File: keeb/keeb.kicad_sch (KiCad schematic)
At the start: 161 parts, among them J101 AVR-ISP-6, J102 USB_C_Receptacle_USB2.0, SW101 SW_Push, SW102 SW_Push, SW103 SW_Push, SW104 SW_Push, SW105 SW_Push, SW106 SW_Push, SW107 SW_Push, SW108 SW_Push, SW109 SW_Push, SW110 SW_Push, SW111 SW_Push, SW112 SW_Push, SW113 SW_Push, SW114 SW_Push, SW115 SW_Push, SW116 SW_Push, SW117 SW_Push, SW118 SW_Push, SW119 SW_Push, SW120 SW_Push, SW121 SW_Push, SW122 SW_Push, SW123 SW_Push, SW124 SW_Push, SW125 SW_Push, SW126 SW_Push, SW127 SW_Push, SW128 SW_Push, SW129 SW_Push, SW130 SW_Push, SW131 SW_Push, SW132 SW_Push, SW133 SW_Push, SW134 SW_Push, SW135 SW_Push, SW136 SW_Push, SW137 SW_Push, SW138 SW_Push, SW139 SW_Push, SW140 SW_Push, SW141 SW_Push, SW142 SW_Push, SW143 SW_Push, SW144 SW_Push, SW145 SW_Push, SW146 SW_Push, SW147 SW_Push, SW148 SW_Push, SW149 SW_Push, SW150 SW_Push, SW151 SW_Push, SW152 SW_Push, SW153 SW_Push, SW154 SW_Push, SW155 SW_Push, SW156 SW_Push, SW157 SW_Push, SW158 SW_Push, SW159 SW_Push, SW160 SW_Push, SW161 SW_Push, SW162 SW_Push, SW163 SW_Push, SW164 SW_Push, SW165 SW_Push, SW166 SW_Push, SW167 SW_Push, U101 ATmega32U4-AU, Y101 16Mhz

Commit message: clean trace
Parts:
- I2C_101, I2C_102: Supplier # (none) -> digi: 839-54-00177CT-ND
- J101: man# digi:839-54-00177CT-ND -> (none)
- J102: Supplier # (none) -> LCSC: C165948; man# LCSC: C165948 -> (none)
- SW101: Supplier # (none) -> LCSC: C231329
- U101: symbol keeb-rescue:ATmega32U4-AU-MCU_Microchip_ATmega -> MCU_Microchip_ATmega:ATmega32U4RC-A; Supplier # (none) -> digi: ATMEGA32U4RC-AU-ND
- Y101: Supplier # (none) -> LCSC: C431146
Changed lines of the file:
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@@
     (pin "2")
   )
-  (symbol (lib_id "keeb-rescue:ATmega32U4-AU-MCU_Microchip_ATmega") (at 228.6 104.775 0) (unit 1)
+  (symbol (lib_id "MCU_Microchip_ATmega:ATmega32U4RC-A") (at 228.6 104.775 0) (unit 1)
     (in_bom yes) (on_board yes)
     (property "Reference" "U101" (id 0) (at 232.41 149.86 0))
@@
     )
     (property "Datasheet" "http://ww1.microchip.com/downloads/en/DeviceDoc/Atmel-7766-8-bit-AVR-ATmega16U4-32U4_Datasheet.pdf" (id 3) (at 228.6 104.775 0)
+      (effects (font (size 1.27 1.27)) hide)
+    )
+    (property "Supplier #" "digi: ATMEGA32U4RC-AU-ND" (id 4) (at 228.6 104.775 0)
       (effects (font (size 1.27 1.27)) hide)
     )
@@
       (effects (font (size 1.27 1.27)) hide)
     )
-    (property "man#" "LCSC: 	C165948" (id 4) (at 36.83 49.53 0)
+    (property "man#" "" (id 4) (at 36.83 49.53 0)
+      (effects (font (size 1.27 1.27)) hide)
+    )
+    (property "Supplier #" "LCSC: C165948" (id 5) (at 36.83 49.53 0)
       (effects (font (size 1.27 1.27)) hide)
     )
@@
       (effects (font (size 1.27 1.27)) hide)
     )
+    (property "Supplier #" "digi: 839-54-00177CT-ND" (id 4) (at 97.155 83.82 0)
+      (effects (font (size 1.27 1.27)) hide)
+    )
     (pin "R1")
     (pin "R2")
@@
       (effects (font (size 1.27 1.27)) hide)
     )
-    (property "man#" "digi:839-54-00177CT-ND" (id 4) (at 92.71 48.26 0)
+    (property "man#" "" (id 4) (at 92.71 48.26 0)
       (effects (font (size 1.27 1.27)) hide)
     )
@@
       (effects (font (size 1.27 1.27)) hide)
     )
+    (property "Supplier #" "digi: 839-54-00177CT-ND" (id 4) (at 65.405 83.82 0)
+      (effects (font (size 1.27 1.27)) hide)
+    )
     (pin "R1")
     (pin "R2")
@@
       (effects (font (size 1.27 1.27)) hide)
     )
-    (property "Datasheet" "~" (id 3) (at 167.64 74.93 0)
+    (property "Datasheet" "https://datasheet.lcsc.com/lcsc/1912111437_YL-Failong-Crystal-9S16000020_C431146.pdf" (id 3) (at 167.64 74.93 0)
+      (effects (font (size 1.27 1.27)) hide)
+    )
+    (property "Supplier #" "LCSC: C431146" (id 4) (at 167.64 74.93 0)
       (effects (font (size 1.27 1.27)) hide)
     )
@@
       (effects (font (size 1.27 1.27)) hide)
     )
-    (property "Datasheet" "~" (id 3) (at 106.045 80.01 0)
+    (property "Datasheet" "" (id 3) (at 106.045 80.01 0)
       (effects (font (size 1.27 1.27)) hide)
     )
@@
       (effects (font (size 1.27 1.27)) hide)
     )
-    (property "Datasheet" "~" (id 3) (at 111.76 80.01 0)
+    (property "Datasheet" "" (id 3) (at 111.76 80.01 0)
       (effects (font (size 1.27 1.27)) hide)
     )
@@
       (effects (font (size 1.27 1.27)) hide)
     )
-    (property "Datasheet" "~" (id 3) (at 74.295 80.01 0)
+    (property "Datasheet" "" (id 3) (at 74.295 80.01 0)
       (effects (font (size 1.27 1.27)) hide)
     )
@@
       (effects (font (size 1.27 1.27)) hide)
     )
-    (property "Datasheet" "~" (id 3) (at 80.01 80.01 0)
+    (property "Datasheet" "" (id 3) (at 80.01 80.01 0)
       (effects (font (size 1.27 1.27)) hide)
     )
@@
       (effects (font (size 1.27 1.27)) hide)
     )
-    (property "Datasheet" "~" (id 3) (at 229.235 42.545 0)
-      (effects (font (size 1.27 1.27)) hide)
-    )
+    (property "Datasheet" "https://datasheet.lcsc.com/lcsc/1810010153_Omron-Electronics-B3U-1000P_C231329.pdf" (id 3) (at 229.235 42.545 0)
+      (effects (font (size 1.27 1.27)) hide)
+    )
+    (property "Supplier #" "LCSC: C231329" (id 4) (at 229.235 37.465 0)
+      (effects (font (size 1.27 1.27)) hide)
+    )

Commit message: qfn layout complete
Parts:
- U101: footprint Package_QFP:TQFP-44_10x10mm_P0.8mm -> Package_DFN_QFN:QFN-44-1EP_7x7mm_P0.5mm_EP5.2x5.2mm
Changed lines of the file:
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@@
     (property "Reference" "U101" (id 0) (at 232.41 149.86 0))
     (property "Value" "ATmega32U4-AU" (id 1) (at 239.395 152.4 0))
-    (property "Footprint" "Package_QFP:TQFP-44_10x10mm_P0.8mm" (id 2) (at 228.6 104.775 0)
+    (property "Footprint" "Package_DFN_QFN:QFN-44-1EP_7x7mm_P0.5mm_EP5.2x5.2mm" (id 2) (at 228.6 104.775 0)
       (effects (font (size 1.27 1.27) italic) hide)
     )
@@
     )
     (path "/00000000-0000-0000-0000-000061b6b293"
-      (reference "U101") (unit 1) (value "ATmega32U4-AU") (footprint "Package_QFP:TQFP-44_10x10mm_P0.8mm")
+      (reference "U101") (unit 1) (value "ATmega32U4-AU") (footprint "Package_DFN_QFN:QFN-44-1EP_7x7mm_P0.5mm_EP5.2x5.2mm")
     )
     (path "/00000000-0000-0000-0000-000061d89e61"

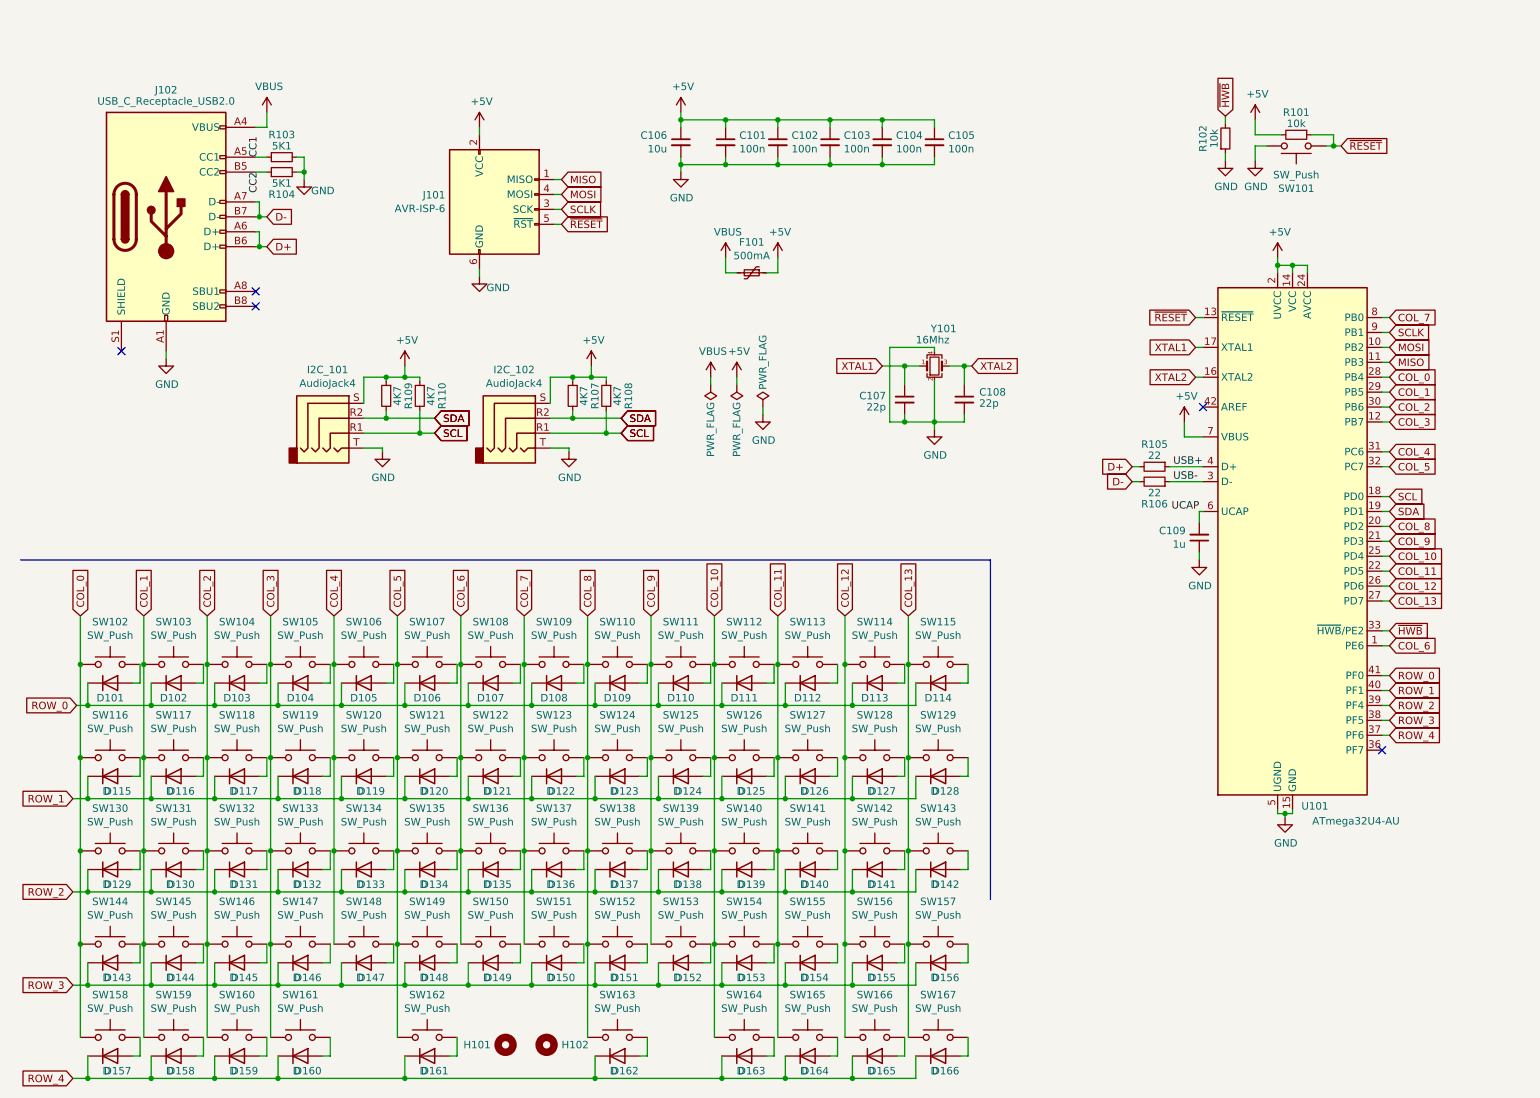
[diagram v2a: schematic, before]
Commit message: trace widths unified
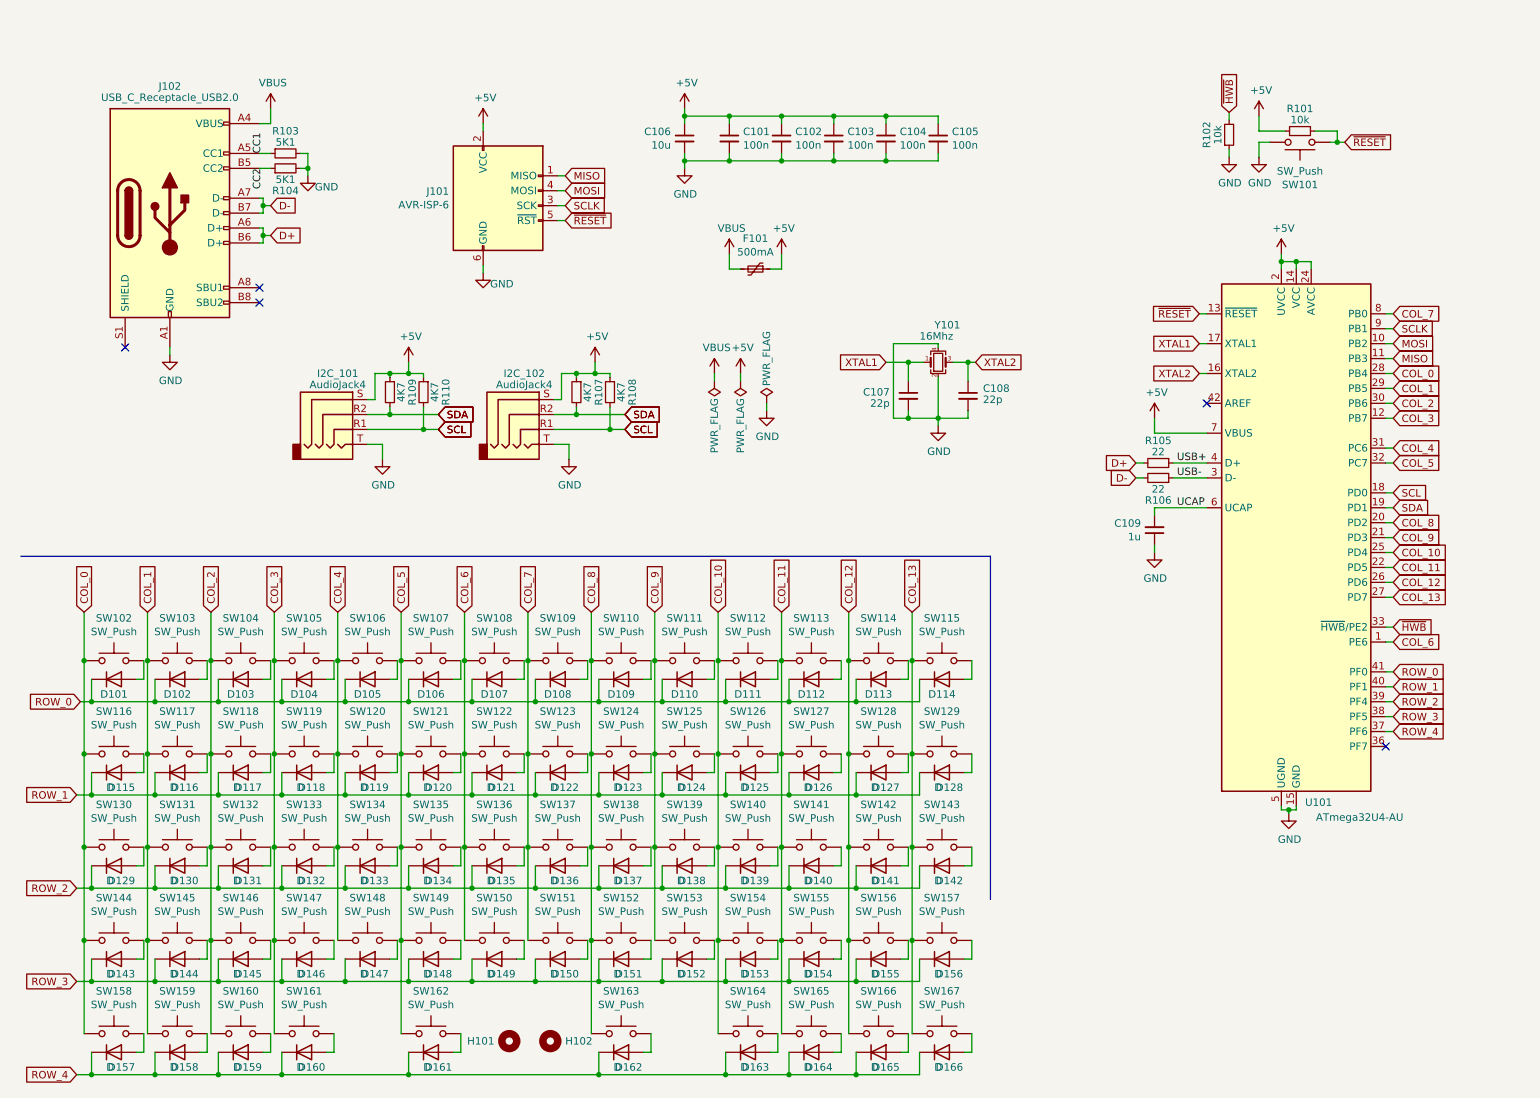
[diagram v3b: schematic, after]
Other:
- moved on the sheet: C101, C102, C103, C104, C105, C106, C107, C108, C109, D101, D102, D103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

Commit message: RESTART: Version2
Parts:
- added U1: TPD2S017, Package_TO_SOT_SMD:SOT-23-6, symbol Power_Protection:TPD2S017
- I2C_101, I2C_102: footprint unORTHOdox_CF:Jack_3.5mm_TIC54-00177_Horizontal -> unORTHOdox:Jack_3.5mm_TIC54-00177_Horizontal
- J101: footprint Connector_PinHeader_2.54mm:PinHeader_2x03_P2.54mm_Vertical -> Stamp_Attach:Stamp-Attach_SA2030-IDC-NL_2x03_P1.27mm_Vertical
- J102: footprint unORTHOdox_CF:USB_C_Receptacle_HRO_TYPE-C-31-M-12 -> unORTHOdox:USB_C_Receptacle_HRO_TYPE-C-31-M-12
- SW102: footprint Switch_Keyboard_Cherry_MX:SW_Cherry_MX_PCB_1.00u -> PCM_Switch_Keyboard_Cherry_MX:SW_Cherry_MX_PCB_1.00u
- U101: footprint Package_DFN_QFN:QFN-44-1EP_7x7mm_P0.5mm_EP5.2x5.2mm -> unORTHOdox:QFN-44-1EP_7x7mm_P0.5mm_EP5.2x5.2mm
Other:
- moved on the sheet: C101, C102, C103, C104, C105, C106, F101, J101, J102, R101, R102, R103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
